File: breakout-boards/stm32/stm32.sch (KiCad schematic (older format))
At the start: 15 parts, among them J1 RJ9, J2 Conn_ARM_JTAG_SWD_10, J3 CONN_LEFT, J4 CONN_RIGHT, P1 USB_C, SW1 SW_Push, U1 AP2127N-3.3, U2 STM32F042K6Tx, Y1 16MHz

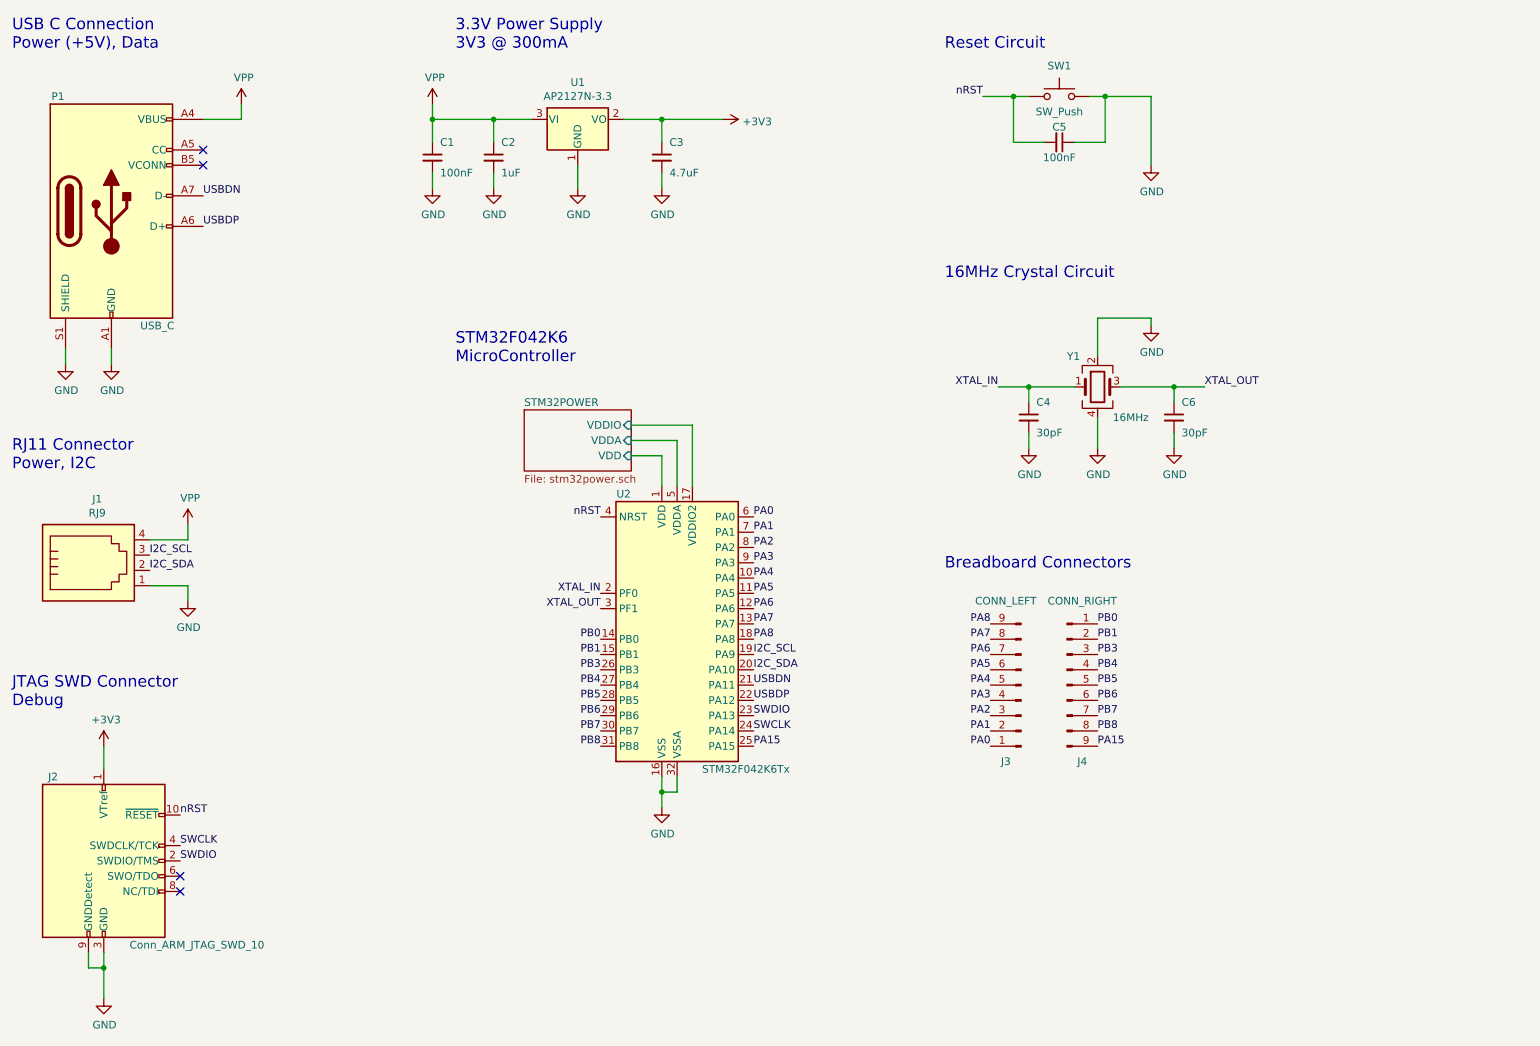
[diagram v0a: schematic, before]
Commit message: (#2) make breakout board for stm32, add 5v sense, reformat pinout, do layout
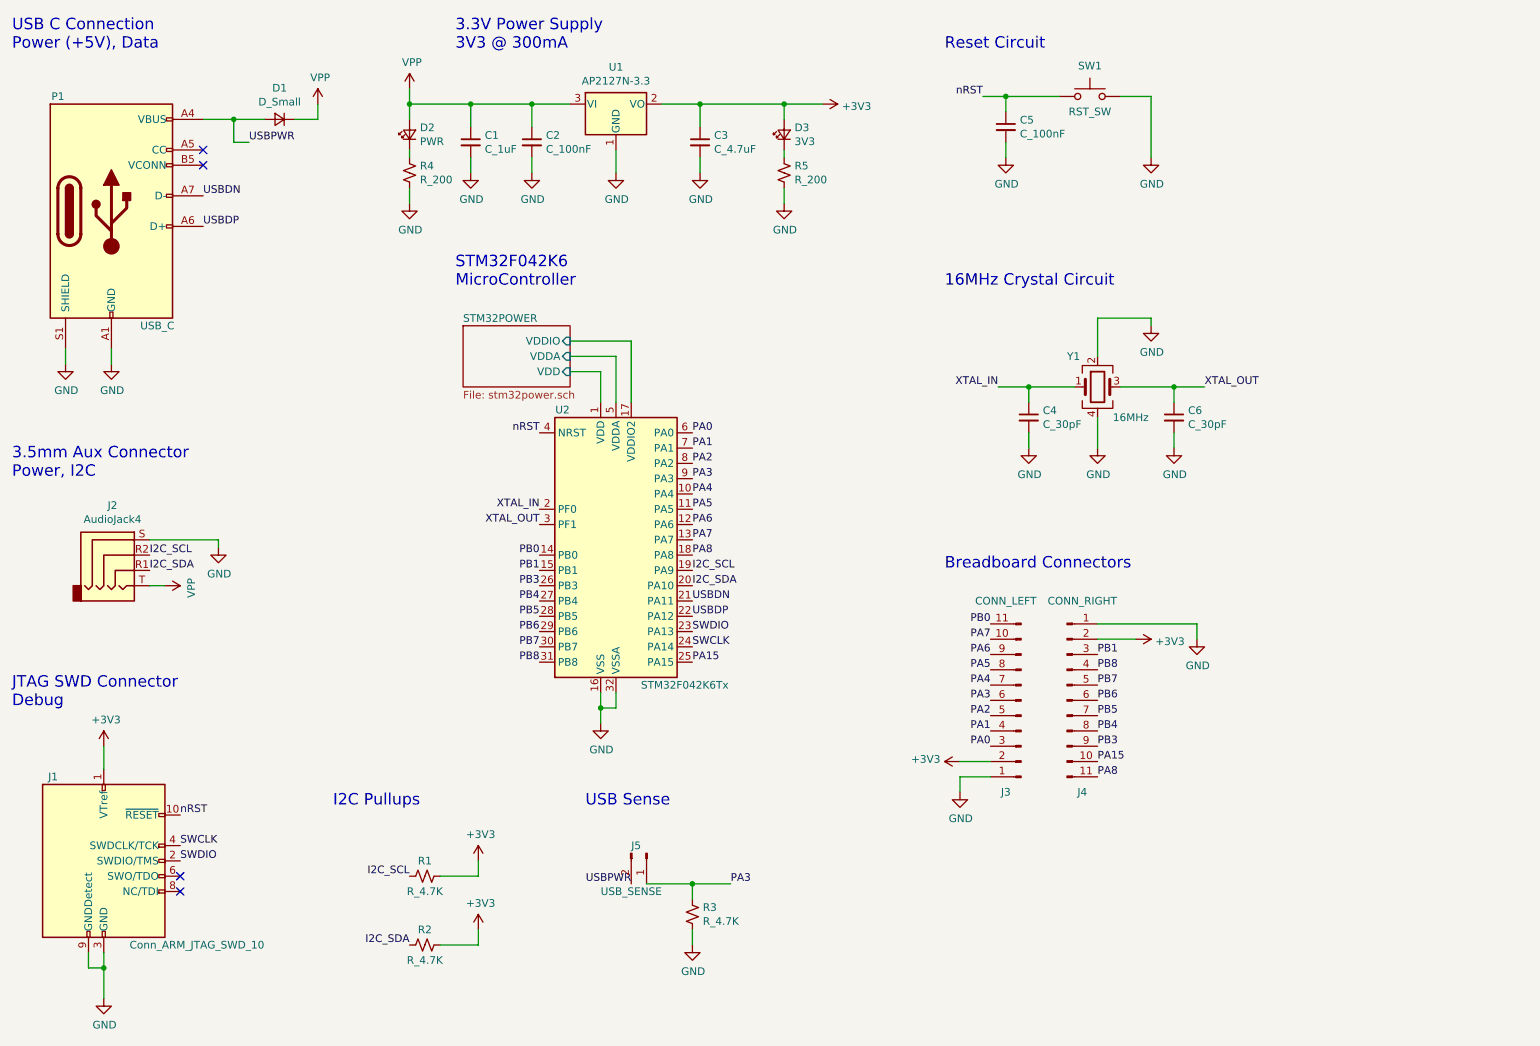
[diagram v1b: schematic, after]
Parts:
- removed C1, C5: 100nF, symbol Device:C_Small
- removed C2: 1uF, symbol Device:C_Small
- removed C3: 4.7uF, symbol Device:C_Small
- removed C4, C6: 30pF, symbol Device:C_Small
- removed J1: RJ9, symbol Connector:RJ9
- removed J3: CONN_LEFT, symbol Connector:Conn_01x09_Male
- removed J4: CONN_RIGHT, symbol Connector:Conn_01x09_Male
- added C1: C_1uF, Capacitor_SMD:C_0402_1005Metric, symbol ultraboard_lib:C_1uF
- added C2, C5: C_100nF, Capacitor_SMD:C_0201_0603Metric, symbol ultraboard_lib:C_100nF
- added C3: C_4.7uF, Capacitor_SMD:C_0402_1005Metric, symbol ultraboard_lib:C_4.7uF
- added C4, C6: C_30pF, Capacitor_SMD:C_0201_0603Metric, symbol ultraboard_lib:C_30pF
- added D1: D_Small, Diode_SMD:D_SMA_Handsoldering, symbol Device:D_Small
- added D2: PWR, LED_SMD:LED_0805_2012Metric, symbol ultraboard_lib:LED_WHT
- added D3: 3V3, LED_SMD:LED_0805_2012Metric, symbol ultraboard_lib:LED_WHT
- added J2: AudioJack4, Connector_Audio:Jack_3.5mm_PJ320D_Horizontal, symbol Connector:AudioJack4
- added J3: CONN_LEFT, Connector_PinSocket_2.54mm:PinSocket_1x11_P2.54mm_Vertical, symbol Connector:Conn_01x11_Male
- added J4: CONN_RIGHT, Connector_PinSocket_2.54mm:PinSocket_1x11_P2.54mm_Vertical, symbol Connector:Conn_01x11_Male
- added J5: USB_SENSE, Connector_PinHeader_2.54mm:PinHeader_1x02_P2.54mm_Vertical, symbol Connector:Conn_01x02_Male
- added R1, R2, R3: R_4.7K, Resistor_SMD:R_0402_1005Metric, symbol ultraboard_lib:R_4.7K
- added R4, R5: R_200, Resistor_SMD:R_0402_1005Metric, symbol ultraboard_lib:R_200
- J1: renamed from J2; footprint (none) -> Connector_PinHeader_1.27mm:PinHeader_2x05_P1.27mm_Vertical_SMD
- P1: footprint (none) -> Connector_USB:USB_C_Receptacle_GCT_USB4085
- SW1: value SW_Push -> RST_SW; footprint (none) -> Button_Switch_THT:SW_PUSH_6mm
- Y1: footprint (none) -> ultraboard:Crystal_SMD_FA238
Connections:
- net +3V3: now also C3.1, D3.2 (A), J3.2 (Pin_2), J4.2 (Pin_2), R1.1, R2.1
- net GND: now also C1.2, C2.2, C3.2, C4.2, C5.2, C6.2, J2.S, J3.1 (Pin_1), J4.1 (Pin_1), R3.2, R4.2, R5.2
- net I2C_SCL: now also J2.R2, R1.2
- net I2C_SDA: now also J2.R1, R2.2
- net PA0: now also J3.3 (Pin_3)
- net PA1: now also J3.4 (Pin_4)
- net PA15: now also J4.10 (Pin_10)
- net PA2: now also J3.5 (Pin_5)
- net PA3: now also J3.6 (Pin_6), J5.1 (Pin_1), R3.1
- net PA4: now also J3.7 (Pin_7)
- net PA5: now also J3.8 (Pin_8)
- net PA6: now also J3.9 (Pin_9)
- net PA7: now also J3.10 (Pin_10)
- net PA8: now also J4.11 (Pin_11)
- net PB0: now also J3.11 (Pin_11)
- net PB1: now also J4.3 (Pin_3)
- net PB3: now also J4.9 (Pin_9)
- net PB4: now also J4.8 (Pin_8)
- net PB5: now also J4.7 (Pin_7)
- net PB6: now also J4.6 (Pin_6)
- net PB7: now also J4.5 (Pin_5)
- net PB8: now also J4.4 (Pin_4)
- net VPP: now also C1.1, C2.1, D1.1 (K), D2.2 (A), J2.T; no longer P1.A4 (VBUS), P1.A9 (VBUS), P1.B4 (VBUS), P1.B9 (VBUS)
- net XTAL_IN: now also C4.1
- net XTAL_OUT: now also C6.1
- net nRST: now also C5.1
- new net: D3.1 (K), R5.1
- new net: D2.1 (K), R4.1
- new net USBPWR: D1.2 (A), J5.2 (Pin_2), P1.A4 (VBUS), P1.A9 (VBUS), P1.B4 (VBUS), P1.B9 (VBUS)
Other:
- note added: "3.5mm Aux Connector\nPower, I2C"
- note added: "I2C Pullups"
- note added: "USB Sense"
- note removed: "RJ11 Connector\nPower, I2C"
- moved on the sheet: SW1, U1, U2

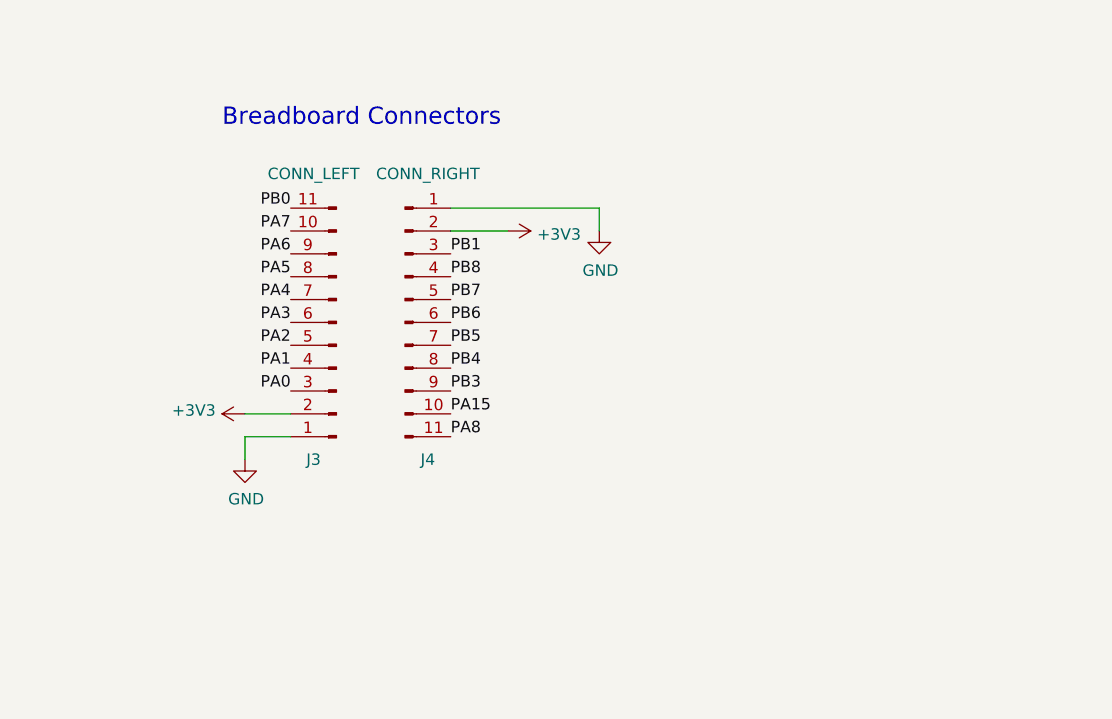
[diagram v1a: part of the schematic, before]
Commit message: (#7) Added I2C to the pin headers and switched 3v3 to 5v
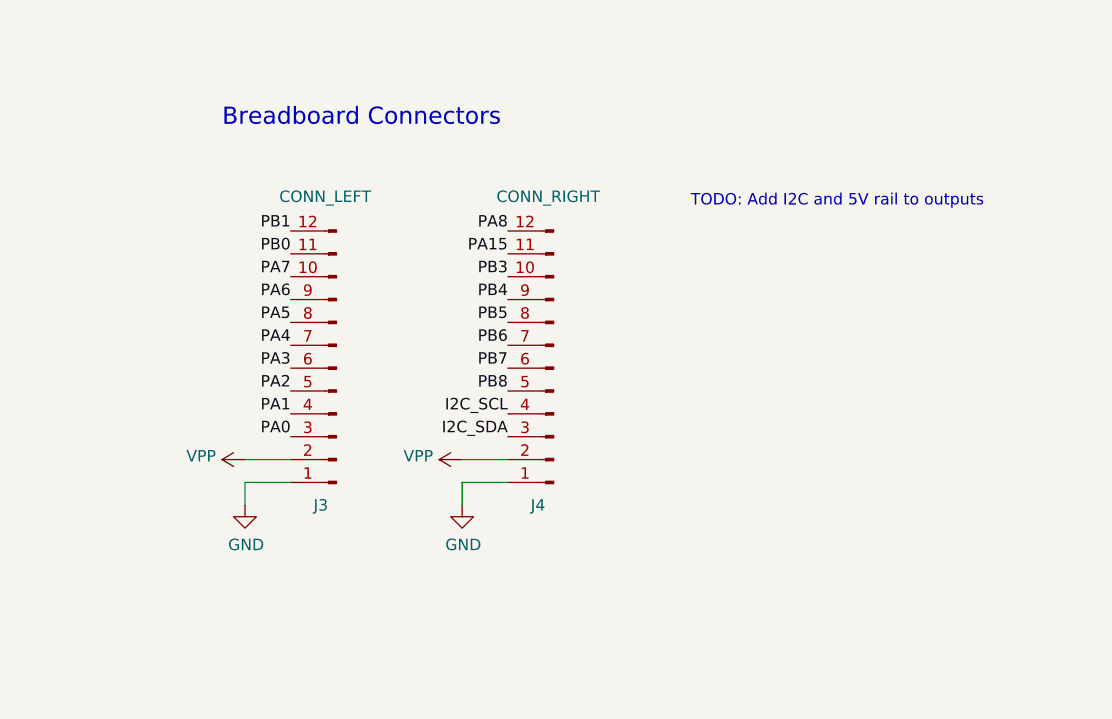
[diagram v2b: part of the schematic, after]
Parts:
- removed J3: CONN_LEFT, Connector_PinSocket_2.54mm:PinSocket_1x11_P2.54mm_Vertical, symbol Connector:Conn_01x11_Male
- removed J4: CONN_RIGHT, Connector_PinSocket_2.54mm:PinSocket_1x11_P2.54mm_Vertical, symbol Connector:Conn_01x11_Male
- added J3: CONN_LEFT, Connector_PinHeader_2.54mm:PinHeader_1x12_P2.54mm_Vertical, symbol Connector:Conn_01x12_Male
- added J4: CONN_RIGHT, Connector_PinHeader_2.54mm:PinHeader_1x12_P2.54mm_Vertical, symbol Connector:Conn_01x12_Male
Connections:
- net GND: now also J3.1 (Pin_1), J4.1 (Pin_1)
- net I2C_SCL: now also J4.4 (Pin_4)
- net I2C_SDA: now also J4.3 (Pin_3)
- net PA0: now also J3.3 (Pin_3)
- net PA1: now also J3.4 (Pin_4)
- net PA15: now also J4.11 (Pin_11)
- net PA2: now also J3.5 (Pin_5)
- net PA3: now also J3.6 (Pin_6)
- net PA4: now also J3.7 (Pin_7)
- net PA5: now also J3.8 (Pin_8)
- net PA6: now also J3.9 (Pin_9)
- net PA7: now also J3.10 (Pin_10)
- net PA8: now also J4.12 (Pin_12)
- net PB0: now also J3.11 (Pin_11)
- net PB1: now also J3.12 (Pin_12)
- net PB3: now also J4.10 (Pin_10)
- net PB4: now also J4.9 (Pin_9)
- net PB5: now also J4.8 (Pin_8)
- net PB6: now also J4.7 (Pin_7)
- net PB7: now also J4.6 (Pin_6)
- net PB8: now also J4.5 (Pin_5)
- net VPP: now also J3.2 (Pin_2), J4.2 (Pin_2)
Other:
- note added: "TODO: Add I2C and 5V rail to outputs"
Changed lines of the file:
@@
 Text Notes 7000 4450 0    75   ~ 0
 Breadboard Connectors
+Text Label 7300 5800 2    50   ~ 0
+PA0
+Text Label 7300 5700 2    50   ~ 0
+PA1
 Text Label 7300 5600 2    50   ~ 0
-PA0
+PA2
 Text Label 7300 5500 2    50   ~ 0
-PA1
+PA3
 Text Label 7300 5400 2    50   ~ 0
-PA2
+PA4
 Text Label 7300 5300 2    50   ~ 0
-PA3
+PA5
 Text Label 7300 5200 2    50   ~ 0
-PA4
+PA6
 Text Label 7300 5100 2    50   ~ 0
-PA5
+PA7
+Text Label 8250 4900 2    50   ~ 0
+PA8
+Text Label 8250 5600 2    50   ~ 0
+PB8
+Text Label 8250 5500 2    50   ~ 0
+PB7
+Text Label 8250 5400 2    50   ~ 0
+PB6
+Text Label 8250 5300 2    50   ~ 0
+PB5
+Text Label 8250 5200 2    50   ~ 0
+PB4
+Text Label 8250 5100 2    50   ~ 0
+PB3
+Text Label 7300 4900 2    50   ~ 0
+PB1
 Text Label 7300 5000 2    50   ~ 0
-PA6
-Text Label 7300 4900 2    50   ~ 0
-PA7
-Text Label 8000 5800 0    50   ~ 0
-PA8
-Text Label 8000 5100 0    50   ~ 0
-PB8
-Text Label 8000 5200 0    50   ~ 0
-PB7
-Text Label 8000 5300 0    50   ~ 0
-PB6
-Text Label 8000 5400 0    50   ~ 0
-PB5
-Text Label 8000 5500 0    50   ~ 0
-PB4
-Text Label 8000 5600 0    50   ~ 0
-PB3
-Text Label 8000 5000 0    50   ~ 0
-PB1
-Text Label 7300 4800 2    50   ~ 0
 PB0
-Text Label 8000 5700 0    50   ~ 0
+Text Label 8250 5000 2    50   ~ 0
 PA15
 $Comp
@@
 	3500 1400 3500 1500
 $Comp
-L Connector:Conn_01x11_Male J4
-U 1 1 5E20C84F
-P 7800 5300
-F 0 "J4" H 7900 4700 50  0000 C CNN
-F 1 "CONN_RIGHT" H 7900 5950 50  0000 C CNN
-F 2 "Connector_PinSocket_2.54mm:PinSocket_1x11_P2.54mm_Vertical" H 7800 5300 50  0001 C CNN
-F 3 "~" H 7800 5300 50  0001 C CNN
-	1    7800 5300
-	1    0    0    -1
-$EndComp
-$Comp
-L Connector:Conn_01x11_Male J3
-U 1 1 5E211A46
-P 7500 5300
-F 0 "J3" H 7600 5900 50  0000 C CNN
-F 1 "CONN_LEFT" H 7600 4650 50  0000 C CNN
-F 2 "Connector_PinSocket_2.54mm:PinSocket_1x11_P2.54mm_Vertical" H 7500 5300 50  0001 C CNN
-F 3 "~" H 7500 5300 50  0001 C CNN
-	1    7500 5300
-	-1   0    0    1
-$EndComp
-$Comp
 L power:GND #PWR037
 U 1 1 5E2132BB
+P 7100 6100
+F 0 "#PWR037" H 7100 5850 50  0001 C CNN
+F 1 "GND" H 7105 5927 50  0000 C CNN
+F 2 "" H 7100 6100 50  0001 C CNN
+F 3 "" H 7100 6100 50  0001 C CNN
+	1    7100 6100
+	1    0    0    -1
+$EndComp
+Wire Wire Line
+	7100 6100 7100 6000
+Wire Wire Line
+	7100 6000 7300 6000
+$Comp
+L power:GND #PWR039
+U 1 1 5E2154DE
+P 8050 6100
+F 0 "#PWR039" H 8050 5850 50  0001 C CNN
+F 1 "GND" H 8055 5927 50  0000 C CNN
+F 2 "" H 8050 6100 50  0001 C CNN
+F 3 "" H 8050 6100 50  0001 C CNN
+	1    8050 6100
+	1    0    0    -1
+$EndComp
+Wire Wire Line
+	8050 6100 8050 6000
+Wire Wire Line
+	7100 5900 7300 5900
+Wire Wire Line
+	8250 5900 8050 5900
+Text Notes 9050 4800 0    50   ~ 0
+TODO: Add I2C and 5V rail to outputs
+Wire Wire Line
+	8050 6000 8250 6000
+$Comp
+L Connector:Conn_01x12_Male J3
+U 1 1 5E16ADD7
+P 7500 5500
+F 0 "J3" H 7600 6100 50  0000 R CNN
+F 1 "CONN_LEFT" H 7750 4750 50  0000 R CNN
+F 2 "Connector_PinHeader_2.54mm:PinHeader_1x12_P2.54mm_Vertical" H 7500 5500 50  0001 C CNN
+F 3 "~" H 7500 5500 50  0001 C CNN
+	1    7500 5500
+	-1   0    0    1
+$EndComp
+$Comp
+L Connector:Conn_01x12_Male J4
+U 1 1 5E16D43E
+P 8450 5500
+F 0 "J4" H 8550 6100 50  0000 R CNN
+F 1 "CONN_RIGHT" H 8700 4750 50  0000 R CNN
+F 2 "Connector_PinHeader_2.54mm:PinHeader_1x12_P2.54mm_Vertical" H 8450 5500 50  0001 C CNN
+F 3 "~" H 8450 5500 50  0001 C CNN
+	1    8450 5500
+	-1   0    0    1
+$EndComp
+Text Label 8250 5800 2    50   ~ 0
+I2C_SDA
+Text Label 8250 5700 2    50   ~ 0
+I2C_SCL
+$Comp
+L power:VPP #PWR?
+U 1 1 5E18CC2A
 P 7100 5900
-F 0 "#PWR037" H 7100 5650 50  0001 C CNN
-F 1 "GND" H 7105 5727 50  0000 C CNN
+F 0 "#PWR?" H 7100 5750 50  0001 C CNN
+F 1 "VPP" V 7115 6027 50  0000 L CNN
 F 2 "" H 7100 5900 50  0001 C CNN
 F 3 "" H 7100 5900 50  0001 C CNN
 	1    7100 5900
-	1    0    0    -1
-$EndComp
-Wire Wire Line
-	7100 5900 7100 5800
-Wire Wire Line
-	7100 5800 7300 5800
-$Comp
-L power:GND #PWR039
-U 1 1 5E2154DE
-P 8650 4900
-F 0 "#PWR039" H 8650 4650 50  0001 C CNN
-F 1 "GND" H 8655 4727 50  0000 C CNN
-F 2 "" H 8650 4900 50  0001 C CNN
-F 3 "" H 8650 4900 50  0001 C CNN
-	1    8650 4900
-	1    0    0    -1
-$EndComp
-Wire Wire Line
-	8650 4900 8650 4800
-Wire Wire Line
-	8650 4800 8000 4800
-$Comp
-L power:+3V3 #PWR036
-U 1 1 5E217601
-P 7100 5700
-F 0 "#PWR036" H 7100 5550 50  0001 C CNN
-F 1 "+3V3" V 7115 5828 50  0000 L CNN
-F 2 "" H 7100 5700 50  0001 C CNN
-F 3 "" H 7100 5700 50  0001 C CNN
-	1    7100 5700
 	0    -1   -1   0
 $EndComp
-Wire Wire Line
-	7100 5700 7300 5700
-$Comp
-L power:+3V3 #PWR038
-U 1 1 5E21A16D
-P 8250 4900
-F 0 "#PWR038" H 8250 4750 50  0001 C CNN
-F 1 "+3V3" V 8265 5028 50  0000 L CNN
-F 2 "" H 8250 4900 50  0001 C CNN
-F 3 "" H 8250 4900 50  0001 C CNN
-	1    8250 4900
-	0    1    1    0
-$EndComp
-Wire Wire Line
-	8000 4900 8250 4900
+$Comp
+L power:VPP #PWR?
+U 1 1 5E18CEEB
+P 8050 5900
+F 0 "#PWR?" H 8050 5750 50  0001 C CNN
+F 1 "VPP" V 8065 6027 50  0000 L CNN
+F 2 "" H 8050 5900 50  0001 C CNN
+F 3 "" H 8050 5900 50  0001 C CNN
+	1    8050 5900
+	0    -1   -1   0
+$EndComp
 $EndSCHEMATC
